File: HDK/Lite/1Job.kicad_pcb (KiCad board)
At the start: 2 copper layers, 48 x 48 mm, 50 parts, among them J201 TERM, J302 DM3CS-SF, J401 SSR, J402 CAN, J403 ANA, J404 PWR, J405 Conn_02x14_Odd_Even, J406 A1-SEL, J407 USB C, U101 STM32G030K6Tx, U102 AMS1117-3.3, U201 SN65HVD230, U202 MCP2518FD, U401 KAQY214, U402 CH340N, Y201 40MHz

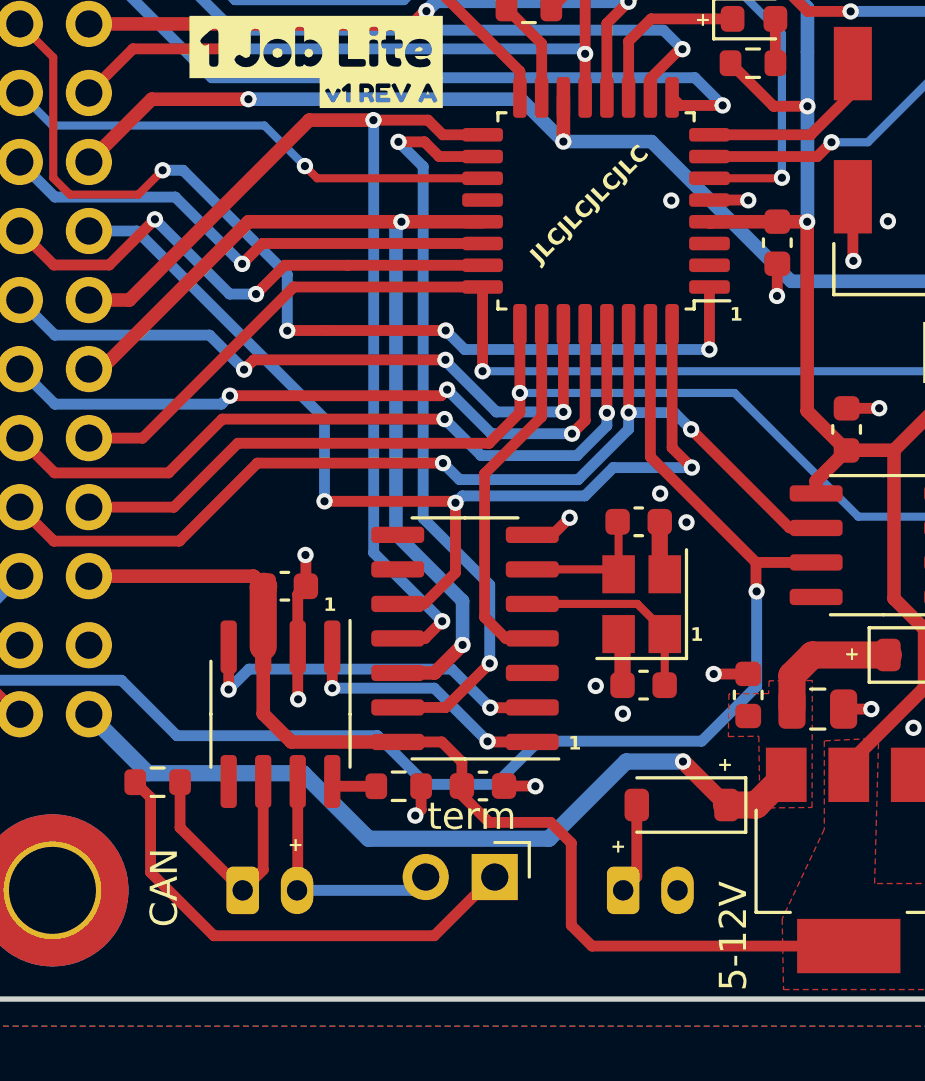
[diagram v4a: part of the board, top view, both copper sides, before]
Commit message: updated 1job silkscreen
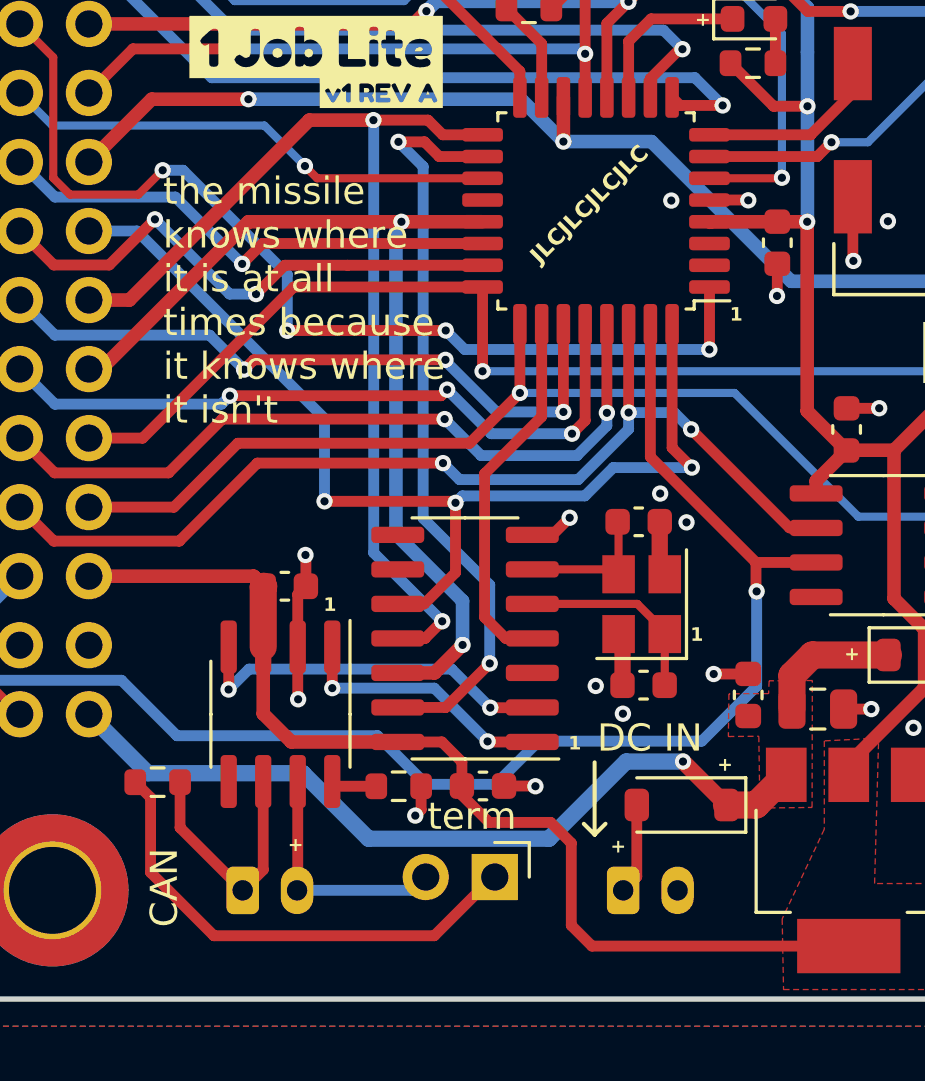
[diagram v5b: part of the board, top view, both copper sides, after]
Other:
- board text added: "DC IN"
- board text added: "the missile knows where it is at all times because it knows where it isn't"
- board text removed: "5-12V"
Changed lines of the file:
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@@
     )
     (stroke (width 0.25) (type solid)) (fill solid) (layer "B.SilkS"))
+  (gr_line (start 100.35 117.55) (end 99.95 117.95)
+    (stroke (width 0.15) (type default)) (layer "F.SilkS"))
+  (gr_line (start 99.95 117.95) (end 99.95 115.29)
+    (stroke (width 0.15) (type default)) (layer "F.SilkS"))
+  (gr_line (start 99.55 117.55) (end 99.95 117.95)
+    (stroke (width 0.15) (type default)) (layer "F.SilkS"))
   (gr_text "QC" (at 103.780001 87.4) (layer "B.SilkS")
     (effects (font (size 1 1) (thickness 0.15)) (justify left bottom mirror))
@@
     (effects (font (size 1 1) (thickness 0.15)) (justify left bottom))
   )
+  (gr_text "the missile \nknows where\nit is at all\ntimes because\nit knows where\nit isn't" (at 84.07 102.91) (layer "F.SilkS")
+    (effects (font (size 1 1) (thickness 0.15)) (justify left bottom))
+  )
   (gr_text "10k" (at 85.27 83.12) (layer "F.SilkS")
     (effects (font (size 0.6 0.6) (thickness 0.15)) (justify left bottom))
@@
     (effects (font (size 0.5 0.5) (thickness 0.125) bold) (justify left bottom))
   )
-  (gr_text "5-12V" (at 105.64 123.71 90) (layer "F.SilkS")
+  (gr_text "DC IN" (at 100.04 114.98) (layer "F.SilkS")
     (effects (font (size 1 1) (thickness 0.15)) (justify left bottom))
   )
@@
   (segment (start 116.829999 114.532501) (end 116.83 114.5325) (width 0.5) (layer "F.Cu") (net 62))
   (segment (start 114.98 114.532501) (end 116.829999 114.532501) (width 0.5) (layer "F.Cu") (net 62))
+  (segment (start 95.349 103.55) (end 86.82 103.55) (width 0.4) (layer "F.Cu") (net 65))
+  (segment (start 86.82 103.55) (end 84.47 105.9) (width 0.4) (layer "F.Cu") (net 65))
+  (segment (start 97.2 101.699) (end 95.349 103.55) (width 0.4) (layer "F.Cu") (net 65))
   (segment (start 84.47 105.9) (end 81.34 105.9) (width 0.4) (layer "F.Cu") (net 65))
-  (segment (start 97.2 102.42) (end 96.07 103.55) (width 0.4) (layer "F.Cu") (net 65))
-  (segment (start 97.2 99.175) (end 97.2 102.42) (width 0.4) (layer "F.Cu") (net 65))
   (segment (start 115.85 106.25) (end 117.455 106.25) (width 0.3) (layer "F.Cu") (net 65))
-  (segment (start 96.07 103.55) (end 86.82 103.55) (width 0.4) (layer "F.Cu") (net 65))
-  (segment (start 86.82 103.55) (end 84.47 105.9) (width 0.4) (layer "F.Cu") (net 65))
+  (segment (start 97.2 99.175) (end 97.2 101.699) (width 0.4) (layer "F.Cu") (net 65))
   (via (at 115.85 106.25) (size 0.6) (drill 0.3) (layers "F.Cu" "B.Cu") (net 65))
   (via (at 97.2 101.699) (size 0.6) (drill 0.3) (layers "F.Cu" "B.Cu") (net 65))
